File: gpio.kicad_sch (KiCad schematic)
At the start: 3 parts, among them J6 Conn_02x06_Odd_Even, U11 TXS0101DBV, U4 AIP74LVC1T45GB236TR

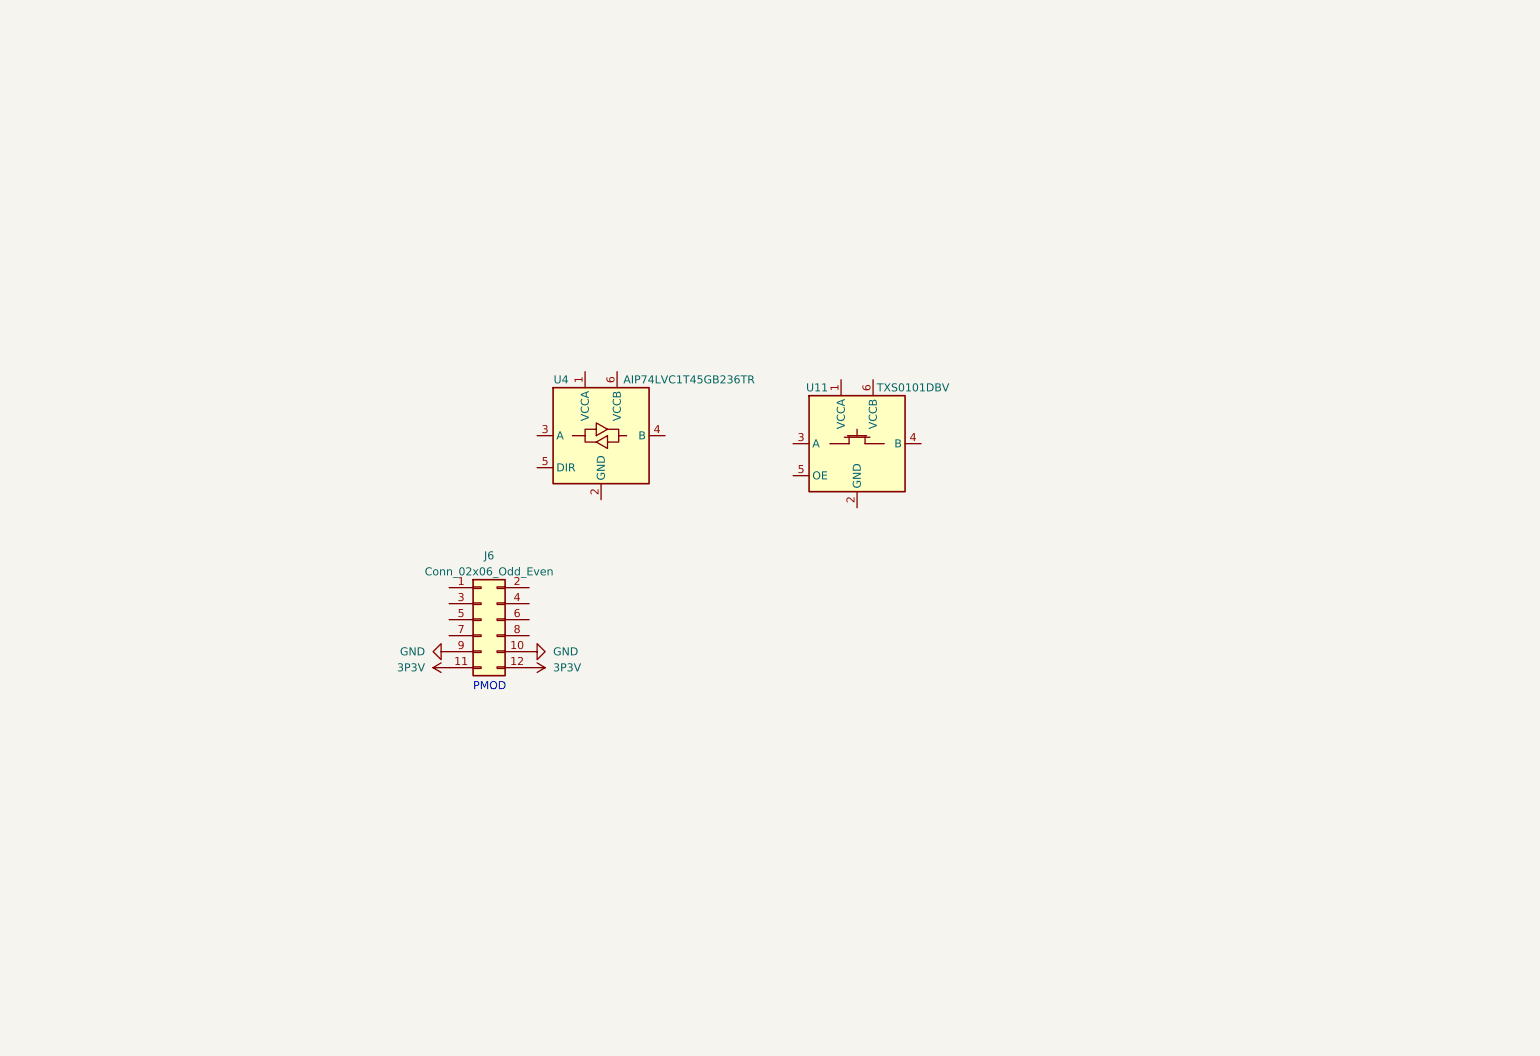
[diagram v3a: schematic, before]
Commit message: gpio.kicad_sch: use TXS02612RTWR as level shifter
Signed-off-by: Huang Rui <vowstar@gmail.com>
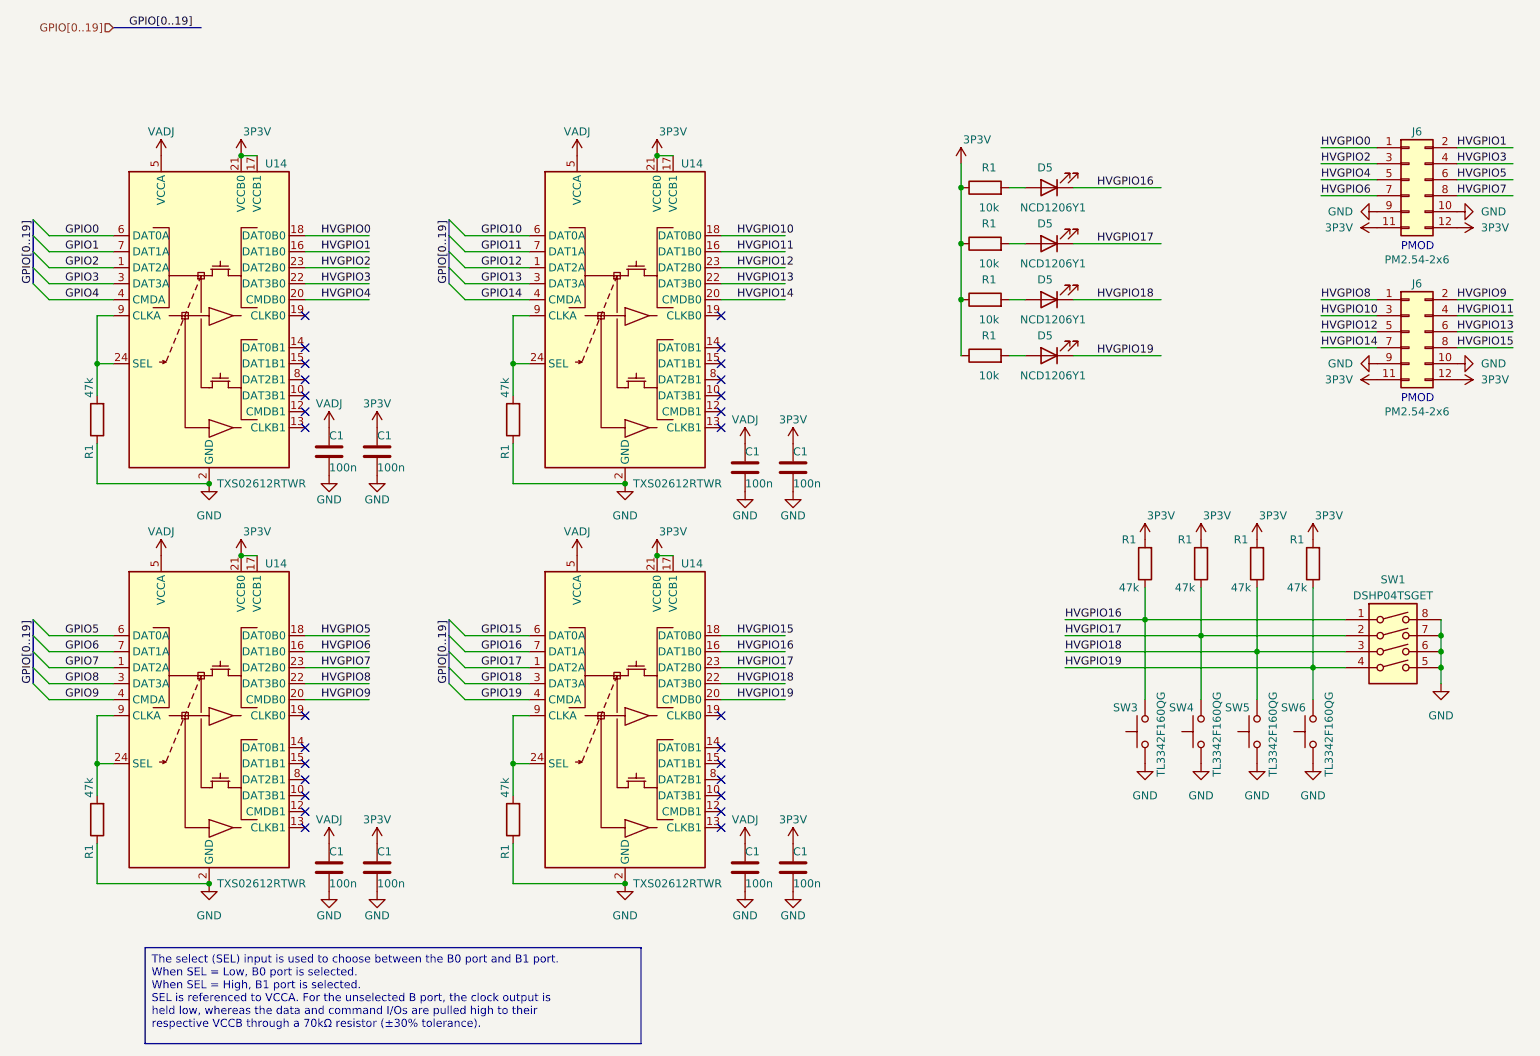
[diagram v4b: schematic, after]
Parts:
- removed U11: TXS0101DBV, Package_TO_SOT_SMD:SOT-23-6, symbol CHIPSAlliance_Logic:TXS0101DBV
- removed U4: AIP74LVC1T45GB236TR, Package_TO_SOT_SMD:SOT-23-6, symbol CHIPSAlliance_Logic:AIP74LVC1T45GB236TR
- added C1 (x8): 100n, Capacitor_SMD:C_0402_1005Metric, symbol Device:C
- added D5 (x4): NCD1206Y1, LED_SMD:LED_1206_3216Metric, symbol Device:LED
- added J6: PM2.54-2x6, Connector_PinHeader_2.54mm:PinHeader_2x06_P2.54mm_Vertical, symbol Connector_Generic:Conn_02x06_Odd_Even
- added R1 (x8): 47k, Resistor_SMD:R_0402_1005Metric, symbol Device:R
- added R1 (x4): 10k, Resistor_SMD:R_0402_1005Metric, symbol Device:R
- added SW1: DSHP04TSGET, Button_Switch_SMD:SW_DIP_SPSTx04_Slide_KingTek_DSHP04TS_W7.62mm_P1.27mm, symbol Switch:SW_DIP_x04
- added SW3, SW4, SW5, SW6: TL3342F160QG, Button_Switch_SMD:SW_SPST_TL3342, symbol Switch:SW_Push
- added U14 (x4): TXS02612RTWR, Package_DFN_QFN:WQFN-24-1EP_4x4mm_P0.5mm_EP2.45x2.45mm, symbol CHIPSAlliance_Logic:TXS02612RTWR
- J6: value Conn_02x06_Odd_Even -> PM2.54-2x6; footprint (none) -> Connector_PinHeader_2.54mm:PinHeader_2x06_P2.54mm_Vertical
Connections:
- net GND: now also C1.2, C1.2, C1.2, C1.2, C1.2, C1.2, C1.2, C1.2, J6.10 (Pin_10), J6.9 (Pin_9), R1.1, R1.1, R1.1, R1.1, SW1.5, SW1.6, SW1.7, SW1.8, SW3.1, SW4.1, SW5.1, SW6.1, U14.11 (GND), U14.11 (GND), U14.11 (GND), U14.11 (GND), U14.2 (GND), U14.2 (GND), U14.2 (GND), U14.2 (GND)
- net P3V3: now also C1.1, C1.1, C1.1, C1.1, C1.1, C1.1, C1.1, C1.1, J6.11 (Pin_11), J6.12 (Pin_12), R1.1, R1.1, R1.1, R1.1, R1.2, R1.2, R1.2, R1.2, U14.17 (VCCB1), U14.17 (VCCB1), U14.17 (VCCB1), U14.17 (VCCB1), U14.21 (VCCB0), U14.21 (VCCB0), U14.21 (VCCB0), U14.21 (VCCB0), U14.5 (VCCA), U14.5 (VCCA), U14.5 (VCCA), U14.5 (VCCA)
- net HVGPIO0: now reaches J6.1 (Pin_1)
- net HVGPIO0: now also U14.18 (DAT0B0)
- net HVGPIO1: now reaches J6.2 (Pin_2)
- net HVGPIO1: now also U14.16 (DAT1B0)
- net HVGPIO2: now reaches J6.3 (Pin_3)
- net HVGPIO2: now also U14.23 (DAT2B0)
- net HVGPIO3: now reaches J6.4 (Pin_4)
- net HVGPIO3: now also U14.22 (DAT3B0)
- net HVGPIO4: now reaches J6.5 (Pin_5)
- net HVGPIO4: now also U14.20 (CMDB0)
- net HVGPIO5: now reaches J6.6 (Pin_6)
- net HVGPIO5: now also U14.18 (DAT0B0)
- net HVGPIO6: now reaches J6.7 (Pin_7)
- net HVGPIO6: now also U14.16 (DAT1B0)
- net HVGPIO7: now reaches J6.8 (Pin_8)
- net HVGPIO7: now also U14.23 (DAT2B0)
- new net: D5.2 (A), R1.2 (x4)
- new net: R1.2, U14.24 (SEL), U14.9 (CLKA) (x4)
- new net GPIO0: U14.6 (DAT0A)
- new net GPIO1: U14.7 (DAT1A)
- new net GPIO10: U14.6 (DAT0A)
- new net GPIO11: U14.7 (DAT1A)
- new net GPIO12: U14.1 (DAT2A)
- new net GPIO13: U14.3 (DAT3A)
- new net GPIO14: U14.4 (CMDA)
- new net GPIO15: U14.6 (DAT0A)
- new net GPIO16: U14.7 (DAT1A)
- new net GPIO17: U14.1 (DAT2A)
- new net GPIO18: U14.3 (DAT3A)
- new net GPIO19: U14.4 (CMDA)
- new net GPIO2: U14.1 (DAT2A)
- new net GPIO3: U14.3 (DAT3A)
- new net GPIO4: U14.4 (CMDA)
- new net GPIO5: U14.6 (DAT0A)
- new net GPIO6: U14.7 (DAT1A)
- new net GPIO7: U14.1 (DAT2A)
- new net GPIO8: U14.3 (DAT3A)
- new net GPIO9: U14.4 (CMDA)
- new net HVGPIO10: J6.3 (Pin_3), U14.18 (DAT0B0)
- new net HVGPIO11: J6.4 (Pin_4), U14.16 (DAT1B0)
- new net HVGPIO12: J6.5 (Pin_5), U14.23 (DAT2B0)
- new net HVGPIO13: J6.6 (Pin_6), U14.22 (DAT3B0)
- new net HVGPIO14: J6.7 (Pin_7), U14.20 (CMDB0)
- new net HVGPIO15: J6.8 (Pin_8), U14.18 (DAT0B0)
- new net HVGPIO16: D5.1 (K), R1.1, SW1.1, SW3.2, U14.16 (DAT1B0)
- new net HVGPIO17: D5.1 (K), R1.1, SW1.2, SW4.2, U14.23 (DAT2B0)
- new net HVGPIO18: D5.1 (K), R1.1, SW1.3, SW5.2, U14.22 (DAT3B0)
- new net HVGPIO19: D5.1 (K), R1.1, SW1.4, SW6.2, U14.20 (CMDB0)
- new net HVGPIO8: J6.1 (Pin_1), U14.22 (DAT3B0)
- new net HVGPIO9: J6.2 (Pin_2), U14.20 (CMDB0)
- no-connect marks 0 -> 28
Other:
- moved on the sheet: J6

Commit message: *.kicad_sch: fix TXS02612RTWR symbols
Signed-off-by: Huang Rui <vowstar@gmail.com>
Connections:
- net GND: now also U14.25 (GND), U14.25 (GND), U14.25 (GND), U14.25 (GND)
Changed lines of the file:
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@@
     (pin "9")
     (pin "1")
+    (pin "25")
     (pin "3")
     (pin "4")
@@
     (pin "9")
     (pin "1")
+    (pin "25")
     (pin "3")
     (pin "4")
@@
     (pin "9")
     (pin "1")
+    (pin "25")
     (pin "3")
     (pin "4")
@@
     (pin "9")
     (pin "1")
+    (pin "25")
     (pin "3")
     (pin "4")
